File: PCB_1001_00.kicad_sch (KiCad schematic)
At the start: 10 parts, among them SW1 SW_MEC_5G_edit, SW2 SW_MEC_5G_edit, SW3 SW_MEC_5G_edit

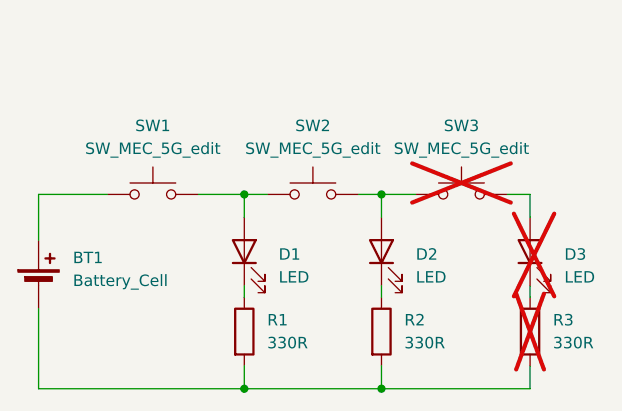
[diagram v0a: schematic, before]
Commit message: Updated file naming to remove spaces
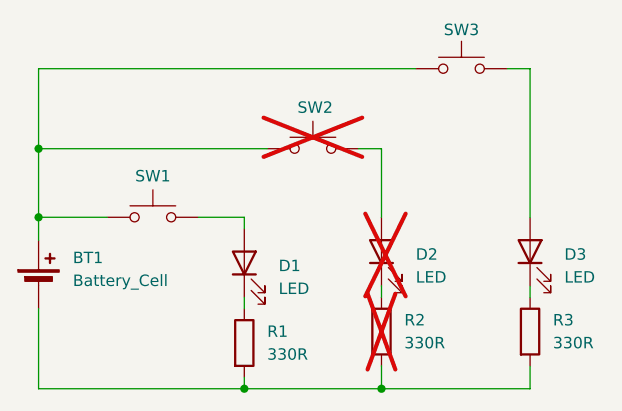
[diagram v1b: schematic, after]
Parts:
- D2, R2, SW2: now not fitted
- D3, R3, SW3: now fitted
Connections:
- net at D2.2 (A), SW2.2 (B): no longer SW3.1 (A)
- net at BT1.1 (+), SW1.1 (A): now also SW2.1 (A), SW3.1 (A)
- net at D1.2 (A), SW1.2 (B): no longer SW2.1 (A)
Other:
- title: (none) -> PCA_1003_00
- moved on the sheet: D1, R1, SW1

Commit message: PCA_1003_01 update in progress. Need top add PCB as component
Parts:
- added PCB1: PCB_1001_02, symbol 00_Sym_Library:00_PCB_Placeholder
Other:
- title: PCA_1003_00 -> PCA_1003
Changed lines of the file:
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@@
 	(paper "A4")
 	(title_block
-		(title "PCA_1003_00")
-		(date "2025-04-01")
-		(rev "00")
+		(title "PCA_1003")
+		(date "2025-04-02")
+		(rev "01")
 	)
 	(junction
@@
 					(unit 1)
 				)
+			)
+		)
+	)
+	(symbol
+		(lib_id "00_Sym_Library:00_PCB_Placeholder")
+		(at 181.61 160.02 0)
+		(unit 1)
+		(exclude_from_sim no)
+		(in_bom yes)
+		(on_board yes)
+		(dnp no)
+		(property "Reference" "PCB1"
+			(at 179.07 160.02 0)
+			(effects
+				(font
+					(size 1.27 1.27)
+				)
+				(justify left)
+			)
+		)
+		(property "Value" "PCB_1001_02"
+			(at 184.404 160.02 0)
+			(effects
+				(font
+					(size 1.27 1.27)
+				)
+				(justify left)
+			)
+		)
+		(property "Footprint" ""
+			(at 181.61 160.02 0)
+			(effects
+				(font
+					(size 1.27 1.27)
+				)
+				(hide yes)
+			)
+		)
+		(property "Datasheet" ""
+			(at 181.61 160.02 0)
+			(effects
+				(font
+					(size 1.27 1.27)
+				)
+				(hide yes)
+			)
+		)
+		(property "Description" ""
+			(at 181.61 160.02 0)
+			(effects
+				(font
+					(size 1.27 1.27)
+				)
+				(hide yes)
+			)
+		)
+		(instances
+			(project ""
+				(path "/9c4608c9-b9d4-4f6a-9cb6-835175086c03"
+					(reference "PCB1")
+					(unit 1)
+				)
